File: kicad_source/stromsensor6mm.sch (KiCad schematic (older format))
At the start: 19 parts, among them CN1 SM04B-SRSS-TB, CN10 CONN_01X01, CN11 CONN_01X01, CN2 SM04B-SRSS-TB, CN20 CONN_01X01, CN21 CONN_01X01, CN3 CONN_01X01, U1 INA226

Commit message: changed mounting holes for connection to wires
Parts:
- CN10, CN20: footprint MECH_mounting_holes:MHP_3.2_5.8 -> MECH_mounting_holes:MHP_6.2_9.0
- CN11, CN21, CN3: footprint MECH_mounting_holes:MHP_3.2_5.8 -> MECH_mounting_holes:MHP_4.0_7.0
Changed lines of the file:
@@
 F 0 "CN10" H 2567 2965 50  0000 C CNN
 F 1 "CONN_01X01" H 2567 2874 50  0000 C CNN
-F 2 "MECH_mounting_holes:MHP_3.2_5.8" H 2650 2750 50  0001 C CNN
+F 2 "MECH_mounting_holes:MHP_6.2_9.0" H 2650 2750 50  0001 C CNN
 F 3 "" H 2650 2750 50  0001 C CNN
 	1    2650 2750
@@
 F 0 "CN20" H 4278 2791 50  0000 L CNN
 F 1 "CONN_01X01" H 4278 2700 50  0000 L CNN
-F 2 "MECH_mounting_holes:MHP_3.2_5.8" H 4200 2750 50  0001 C CNN
+F 2 "MECH_mounting_holes:MHP_6.2_9.0" H 4200 2750 50  0001 C CNN
 F 3 "" H 4200 2750 50  0001 C CNN
 	1    4200 2750
@@
 F 0 "CN21" H 4278 2991 50  0000 L CNN
 F 1 "CONN_01X01" H 4278 2900 50  0000 L CNN
-F 2 "MECH_mounting_holes:MHP_3.2_5.8" H 4200 2950 50  0001 C CNN
+F 2 "MECH_mounting_holes:MHP_4.0_7.0" H 4200 2950 50  0001 C CNN
 F 3 "" H 4200 2950 50  0001 C CNN
 	1    4200 2950
@@
 F 0 "CN11" H 2567 3165 50  0000 C CNN
 F 1 "CONN_01X01" H 2567 3074 50  0000 C CNN
-F 2 "MECH_mounting_holes:MHP_3.2_5.8" H 2650 2950 50  0001 C CNN
+F 2 "MECH_mounting_holes:MHP_4.0_7.0" H 2650 2950 50  0001 C CNN
 F 3 "" H 2650 2950 50  0001 C CNN
 	1    2650 2950
@@
 F 0 "CN3" H 3878 4891 50  0000 L CNN
 F 1 "CONN_01X01" H 3878 4800 50  0000 L CNN
-F 2 "MECH_mounting_holes:MHP_3.2_5.8" H 3800 4850 50  0001 C CNN
+F 2 "MECH_mounting_holes:MHP_4.0_7.0" H 3800 4850 50  0001 C CNN
 F 3 "" H 3800 4850 50  0001 C CNN
 	1    3800 4850

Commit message: changed current sensor to more robust part
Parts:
- added R20: BR3FB5L00, resistors:BR3, symbol devices:R_0603
- R10: renamed from R1; value 5 mOhm -> BR3FB5L00; footprint resistors:R_0603 -> resistors:BR3
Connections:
- wire segments 85 -> 89
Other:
- note added: "5 mOhm for measurements \n-16.384A to +16.384A\n\nplace second resistor (R20)\n5 mOhm for measurements \n-32.768A to +32.768A"
- note removed: "5 mOhm for measurements \n-16.384A to +16.384A"
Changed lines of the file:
@@
 	3900 4000 3900 4050
 $Comp
-L devices:R_0603 R1
+L devices:R_0603 R10
 U 1 1 5F22A062
 P 3500 2750
-F 0 "R1" V 3304 2750 50  0000 C CNN
-F 1 "5 mOhm" V 3395 2750 50  0000 C CNN
-F 2 "resistors:R_0603" H 3500 2600 50  0001 C CNN
+F 0 "R10" V 3304 2750 50  0000 C CNN
+F 1 "BR3FB5L00" V 3395 2750 50  0000 C CNN
+F 2 "resistors:BR3" H 3500 2600 50  0001 C CNN
 F 3 "" H 3500 2750 50  0000 C CNN
 	1    3500 2750
@@
 	3950 3900 3800 3900
 Wire Wire Line
-	3800 3900 3800 2750
+	3800 3900 3800 3050
 Connection ~ 3800 2750
 Wire Wire Line
@@
 	3950 3500 3900 3500
 Wire Wire Line
-	3150 3500 3150 2750
+	3150 3500 3150 3050
 Connection ~ 3150 2750
 Wire Wire Line
@@
 	3550 4850 3550 4900
 Text Notes 3000 2400 0    50   ~ 0
-5 mOhm for measurements \n-16.384A to +16.384A
+5 mOhm for measurements \n-16.384A to +16.384A\n\nplace second resistor (R20)\n5 mOhm for measurements \n-32.768A to +32.768A
+$Comp
+L devices:R_0603 R20
+U 1 1 5F21ED20
+P 3500 3050
+F 0 "R20" V 3304 3050 50  0000 C CNN
+F 1 "BR3FB5L00" V 3395 3050 50  0000 C CNN
+F 2 "resistors:BR3" H 3500 2900 50  0001 C CNN
+F 3 "" H 3500 3050 50  0000 C CNN
+	1    3500 3050
+	0    1    1    0
+$EndComp
+Wire Wire Line
+	3600 3050 3800 3050
+Connection ~ 3800 3050
+Wire Wire Line
+	3800 3050 3800 2750
+Wire Wire Line
+	3400 3050 3150 3050
+Connection ~ 3150 3050
+Wire Wire Line
+	3150 3050 3150 2750
 $EndSCHEMATC

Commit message: changed dip switch, updated placement and pcb shape
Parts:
- S1: footprint mechanical-switches:dip_8-300 -> mechanical-switches:WE_416131160808
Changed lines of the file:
@@
 F 0 "S1" H 6600 5575 50  0000 C CNN
 F 1 "SW_DIP_x8" H 6600 5484 50  0000 C CNN
-F 2 "mechanical-switches:dip_8-300" H 6550 5000 50  0001 C CNN
+F 2 "mechanical-switches:WE_416131160808" H 6550 5000 50  0001 C CNN
 F 3 "http://www.ctscorp.com/components/Datasheets/206-208.pdf" H 6600 5483 50  0001 C CNN
 	1    6600 5000

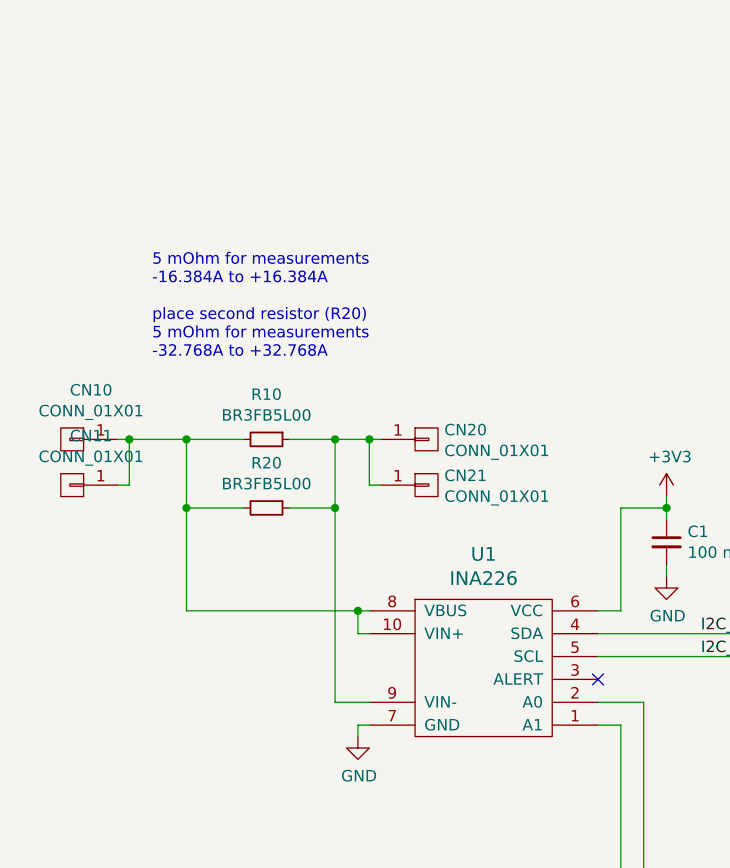
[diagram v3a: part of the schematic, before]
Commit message: updated layout, added decoupling capacitor on current sense
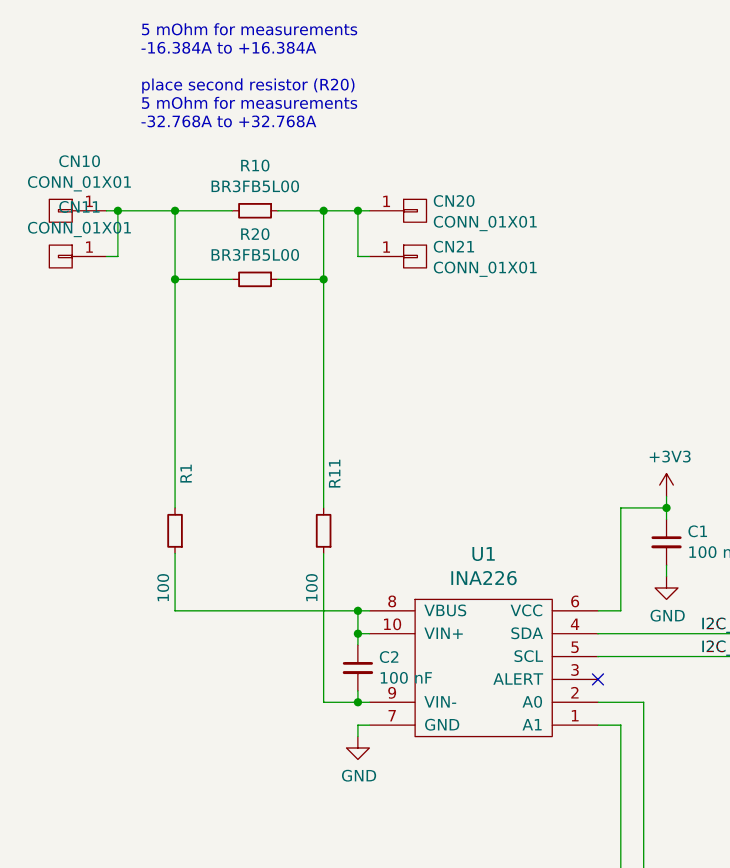
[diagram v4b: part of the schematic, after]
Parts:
- added C2: 100 nF, capacitors:C_0603, symbol devices:C_0603
- added R1, R11: 100, resistors:R_0603, symbol devices:R_0603
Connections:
- wire segments 89 -> 94
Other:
- moved on the sheet: CN10, CN11, CN20, CN21, R10, R20
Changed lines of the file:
@@
 L mechanical-connectors:CONN_01X01 CN10
 U 1 1 5F20C1E3
-P 2650 2750
-F 0 "CN10" H 2567 2965 50  0000 C CNN
-F 1 "CONN_01X01" H 2567 2874 50  0000 C CNN
-F 2 "MECH_mounting_holes:MHP_6.2_9.0" H 2650 2750 50  0001 C CNN
-F 3 "" H 2650 2750 50  0001 C CNN
-	1    2650 2750
+P 2600 1750
+F 0 "CN10" H 2517 1965 50  0000 C CNN
+F 1 "CONN_01X01" H 2517 1874 50  0000 C CNN
+F 2 "MECH_mounting_holes:MHP_6.2_9.0" H 2600 1750 50  0001 C CNN
+F 3 "" H 2600 1750 50  0001 C CNN
+	1    2600 1750
 	-1   0    0    -1
 $EndComp
@@
 L devices:R_0603 R10
 U 1 1 5F22A062
-P 3500 2750
-F 0 "R10" V 3304 2750 50  0000 C CNN
-F 1 "BR3FB5L00" V 3395 2750 50  0000 C CNN
-F 2 "resistors:BR3" H 3500 2600 50  0001 C CNN
-F 3 "" H 3500 2750 50  0000 C CNN
-	1    3500 2750
+P 3450 1750
+F 0 "R10" V 3254 1750 50  0000 C CNN
+F 1 "BR3FB5L00" V 3345 1750 50  0000 C CNN
+F 2 "resistors:BR3" H 3450 1600 50  0001 C CNN
+F 3 "" H 3450 1750 50  0000 C CNN
+	1    3450 1750
 	0    1    1    0
 $EndComp
@@
 L mechanical-connectors:CONN_01X01 CN20
 U 1 1 5F22AC67
-P 4200 2750
-F 0 "CN20" H 4278 2791 50  0000 L CNN
-F 1 "CONN_01X01" H 4278 2700 50  0000 L CNN
-F 2 "MECH_mounting_holes:MHP_6.2_9.0" H 4200 2750 50  0001 C CNN
-F 3 "" H 4200 2750 50  0001 C CNN
-	1    4200 2750
+P 4150 1750
+F 0 "CN20" H 4228 1791 50  0000 L CNN
+F 1 "CONN_01X01" H 4228 1700 50  0000 L CNN
+F 2 "MECH_mounting_holes:MHP_6.2_9.0" H 4150 1750 50  0001 C CNN
+F 3 "" H 4150 1750 50  0001 C CNN
+	1    4150 1750
 	1    0    0    -1
 $EndComp
@@
 L mechanical-connectors:CONN_01X01 CN21
 U 1 1 5F22AF77
-P 4200 2950
-F 0 "CN21" H 4278 2991 50  0000 L CNN
-F 1 "CONN_01X01" H 4278 2900 50  0000 L CNN
-F 2 "MECH_mounting_holes:MHP_4.0_7.0" H 4200 2950 50  0001 C CNN
-F 3 "" H 4200 2950 50  0001 C CNN
-	1    4200 2950
+P 4150 1950
+F 0 "CN21" H 4228 1991 50  0000 L CNN
+F 1 "CONN_01X01" H 4228 1900 50  0000 L CNN
+F 2 "MECH_mounting_holes:MHP_4.0_7.0" H 4150 1950 50  0001 C CNN
+F 3 "" H 4150 1950 50  0001 C CNN
+	1    4150 1950
 	1    0    0    -1
 $EndComp
@@
 L mechanical-connectors:CONN_01X01 CN11
 U 1 1 5F22C000
-P 2650 2950
-F 0 "CN11" H 2567 3165 50  0000 C CNN
-F 1 "CONN_01X01" H 2567 3074 50  0000 C CNN
-F 2 "MECH_mounting_holes:MHP_4.0_7.0" H 2650 2950 50  0001 C CNN
-F 3 "" H 2650 2950 50  0001 C CNN
-	1    2650 2950
+P 2600 1950
+F 0 "CN11" H 2517 2165 50  0000 C CNN
+F 1 "CONN_01X01" H 2517 2074 50  0000 C CNN
+F 2 "MECH_mounting_holes:MHP_4.0_7.0" H 2600 1950 50  0001 C CNN
+F 3 "" H 2600 1950 50  0001 C CNN
+	1    2600 1950
 	-1   0    0    -1
 $EndComp
 Wire Wire Line
-	2850 2750 2900 2750
-Wire Wire Line
-	4000 2750 3950 2750
-Wire Wire Line
-	3950 2950 3950 2750
-Connection ~ 3950 2750
-Wire Wire Line
-	3950 2750 3800 2750
-Wire Wire Line
-	4000 2950 3950 2950
-Wire Wire Line
-	2850 2950 2900 2950
-Wire Wire Line
-	2900 2950 2900 2750
-Connection ~ 2900 2750
-Wire Wire Line
-	2900 2750 3150 2750
-Wire Wire Line
-	3950 3900 3800 3900
-Wire Wire Line
-	3800 3900 3800 3050
-Connection ~ 3800 2750
-Wire Wire Line
-	3800 2750 3600 2750
+	2800 1750 2850 1750
+Wire Wire Line
+	3950 1750 3900 1750
+Wire Wire Line
+	3900 1950 3900 1750
+Connection ~ 3900 1750
+Wire Wire Line
+	3900 1750 3750 1750
+Wire Wire Line
+	3950 1950 3900 1950
+Wire Wire Line
+	2800 1950 2850 1950
+Wire Wire Line
+	2850 1950 2850 1750
+Connection ~ 2850 1750
+Wire Wire Line
+	2850 1750 3100 1750
+Connection ~ 3750 1750
+Wire Wire Line
+	3750 1750 3550 1750
 Wire Wire Line
 	3950 3500 3900 3500
-Wire Wire Line
-	3150 3500 3150 3050
-Connection ~ 3150 2750
-Wire Wire Line
-	3150 2750 3400 2750
+Connection ~ 3100 1750
+Wire Wire Line
+	3100 1750 3350 1750
 Wire Wire Line
 	3950 3600 3900 3600
@@
 	3900 3600 3900 3500
 Connection ~ 3900 3500
-Wire Wire Line
-	3900 3500 3150 3500
 Wire Wire Line
 	8000 2500 8900 2500
@@
 Wire Wire Line
 	3550 4850 3550 4900
-Text Notes 3000 2400 0    50   ~ 0
+Text Notes 2950 1400 0    50   ~ 0
 5 mOhm for measurements \n-16.384A to +16.384A\n\nplace second resistor (R20)\n5 mOhm for measurements \n-32.768A to +32.768A
 $Comp
 L devices:R_0603 R20
 U 1 1 5F21ED20
-P 3500 3050
-F 0 "R20" V 3304 3050 50  0000 C CNN
-F 1 "BR3FB5L00" V 3395 3050 50  0000 C CNN
-F 2 "resistors:BR3" H 3500 2900 50  0001 C CNN
-F 3 "" H 3500 3050 50  0000 C CNN
-	1    3500 3050
-	0    1    1    0
-$EndComp
-Wire Wire Line
-	3600 3050 3800 3050
-Connection ~ 3800 3050
-Wire Wire Line
-	3800 3050 3800 2750
-Wire Wire Line
-	3400 3050 3150 3050
-Connection ~ 3150 3050
-Wire Wire Line
-	3150 3050 3150 2750
+P 3450 2050
+F 0 "R20" V 3254 2050 50  0000 C CNN
+F 1 "BR3FB5L00" V 3345 2050 50  0000 C CNN
+F 2 "resistors:BR3" H 3450 1900 50  0001 C CNN
+F 3 "" H 3450 2050 50  0000 C CNN
+	1    3450 2050
+	0    1    1    0
+$EndComp
+Wire Wire Line
+	3550 2050 3750 2050
+Connection ~ 3750 2050
+Wire Wire Line
+	3750 2050 3750 1750
+Wire Wire Line
+	3350 2050 3100 2050
+Connection ~ 3100 2050
+Wire Wire Line
+	3100 2050 3100 1750
+$Comp
+L devices:C_0603 C2
+U 1 1 5F22800E
+P 3900 3750
+F 0 "C2" H 3992 3796 50  0000 L CNN
+F 1 "100 nF" H 3992 3705 50  0000 L CNN
+F 2 "capacitors:C_0603" H 3900 3600 50  0001 C CNN
+F 3 "" H 3900 3750 50  0000 C CNN
+	1    3900 3750
+	1    0    0    -1
+$EndComp
+$Comp
+L devices:R_0603 R11
+U 1 1 5F228386
+P 3750 3150
+F 0 "R11" V 3700 2900 50  0000 C CNN
+F 1 "100" V 3800 3400 50  0000 C CNN
+F 2 "resistors:R_0603" H 3750 3000 50  0001 C CNN
+F 3 "" H 3750 3150 50  0000 C CNN
+	1    3750 3150
+	-1   0    0    1
+$EndComp
+$Comp
+L devices:R_0603 R1
+U 1 1 5F2296E5
+P 3100 3150
+F 0 "R1" V 3050 2900 50  0000 C CNN
+F 1 "100" V 3150 3400 50  0000 C CNN
+F 2 "resistors:R_0603" H 3100 3000 50  0001 C CNN
+F 3 "" H 3100 3150 50  0000 C CNN
+	1    3100 3150
+	-1   0    0    1
+$EndComp
+Wire Wire Line
+	3100 2050 3100 3050
+Wire Wire Line
+	3100 3250 3100 3500
+Wire Wire Line
+	3100 3500 3900 3500
+Wire Wire Line
+	3750 2050 3750 3050
+Wire Wire Line
+	3750 3250 3750 3900
+Wire Wire Line
+	3750 3900 3900 3900
+Wire Wire Line
+	3900 3850 3900 3900
+Connection ~ 3900 3900
+Wire Wire Line
+	3900 3900 3950 3900
+Wire Wire Line
+	3900 3650 3900 3600
+Connection ~ 3900 3600
 $EndSCHEMATC

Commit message: finished layout
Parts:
- added L1: Label, labels:generationmake_small_silk, symbol devices:Label
- added R12, R13: DNI, resistors:R_0603, symbol devices:R_0603
- S1: value SW_DIP_x8 -> 218-8LPST
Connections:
- net labels added: A0, A1, IN, IN_R, OUT, OUT_R
- wire segments 94 -> 100
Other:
- moved on the sheet: C2, CN10, CN11, CN20, CN21, R1, R10, R11, R20

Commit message: current sensor input filtering works not as intended, changed R1 and R11 to 0 Ohm
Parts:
- R1, R11: value 100 -> 0R
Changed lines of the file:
@@
 P 3200 3150
 F 0 "R11" H 3050 3100 50  0000 C CNN
-F 1 "100" H 3050 3200 50  0000 C CNN
+F 1 "0R" H 3050 3200 50  0000 C CNN
 F 2 "resistors:R_0603" H 3200 3000 50  0001 C CNN
 F 3 "" H 3200 3150 50  0000 C CNN
@@
 P 2550 3150
 F 0 "R1" H 2450 3100 50  0000 C CNN
-F 1 "100" H 2400 3200 50  0000 C CNN
+F 1 "0R" H 2400 3200 50  0000 C CNN
 F 2 "resistors:R_0603" H 2550 3000 50  0001 C CNN
 F 3 "" H 2550 3150 50  0000 C CNN

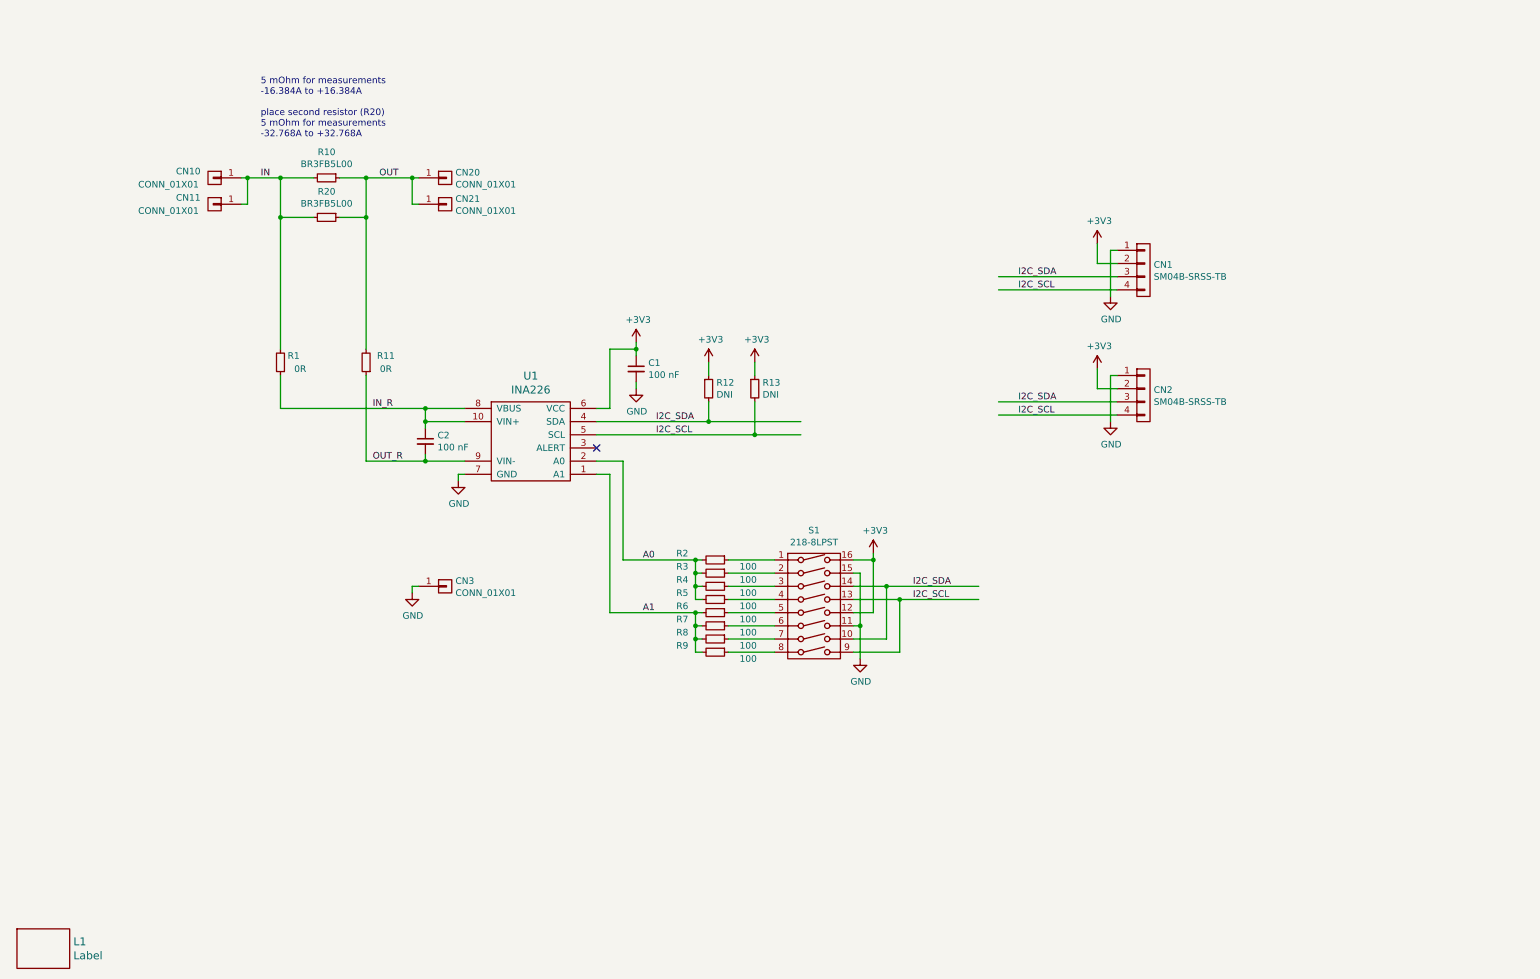
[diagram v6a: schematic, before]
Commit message: added description and documentation in schematic and layout, added pdfs
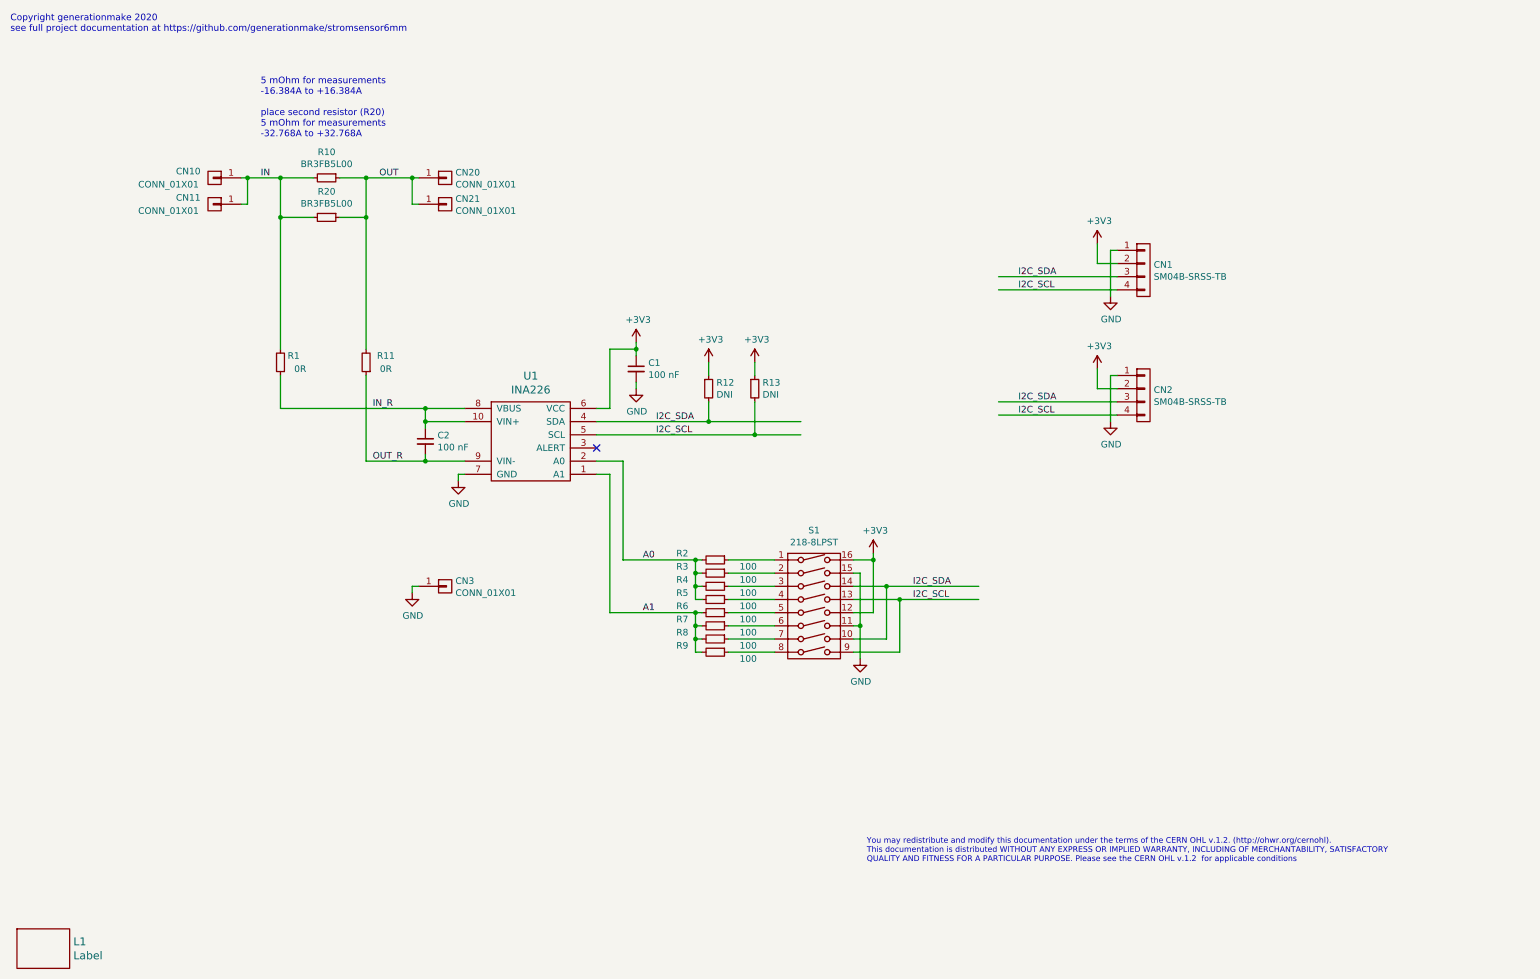
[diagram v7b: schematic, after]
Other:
- note added: "Copyright generationmake 2020\nsee full project documentation at https://github.com/generationmake/stromsensor6mm"
- note added: "You may redistribute and modify this documentation under the terms of the CERN OHL v.1.2. (http://ohwr.org/cernohl). \nThis documentation is distributed WITHOUT ANY EXPRESS OR IMPLIED WARRANTY, INCLUDING OF MERCHANTABILITY, SATISFACTORY \nQUALITY AND FITNESS FOR A PARTICULAR PURPOSE. Please see the CERN OHL v.1.2 for applicable conditions"
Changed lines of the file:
@@
 encoding utf-8
 Sheet 1 1
-Title ""
-Date ""
-Rev ""
-Comp ""
+Title "Stromsensor6mm"
+Date "2020-08-30"
+Rev "0.1"
+Comp "generationmake"
 Comment1 ""
 Comment2 ""
 Comment3 ""
-Comment4 ""
+Comment4 "This documentation describes Open Hardware and is licensed under the CERN OHL v. 1.2."
 $EndDescr
 $Comp
@@
 	1    0    0    -1
 $EndComp
+Text Notes 500  650  0    50   ~ 0
+Copyright generationmake 2020\nsee full project documentation at https://github.com/generationmake/stromsensor6mm
+Text Notes 7000 6950 0    43   ~ 0
+You may redistribute and modify this documentation under the terms of the CERN OHL v.1.2. (http://ohwr.org/cernohl). \nThis documentation is distributed WITHOUT ANY EXPRESS OR IMPLIED WARRANTY, INCLUDING OF MERCHANTABILITY, SATISFACTORY \nQUALITY AND FITNESS FOR A PARTICULAR PURPOSE. Please see the CERN OHL v.1.2  for applicable conditions
 $EndSCHEMATC
